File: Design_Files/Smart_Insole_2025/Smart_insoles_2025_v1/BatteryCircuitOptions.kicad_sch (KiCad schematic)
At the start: 23 parts, among them J4 S2B-PH-SM4-TB_LF__SN_, Q2 FDN306P, U1 ME6211C33M5, U7 BQ24040DSQR

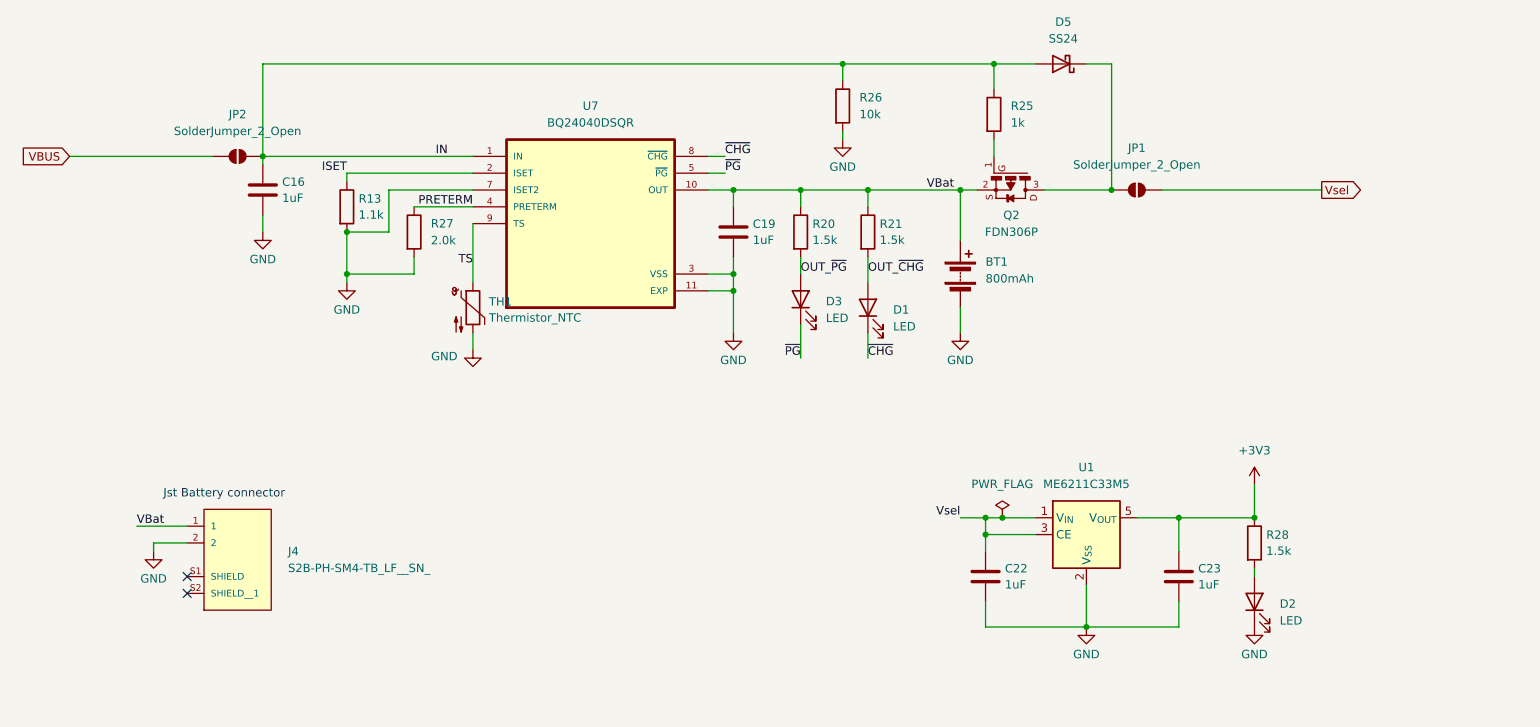
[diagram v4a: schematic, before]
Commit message: SCH: Added test points on idle MCU pins and Power supply. Added ON/OFF switch on VSEL.
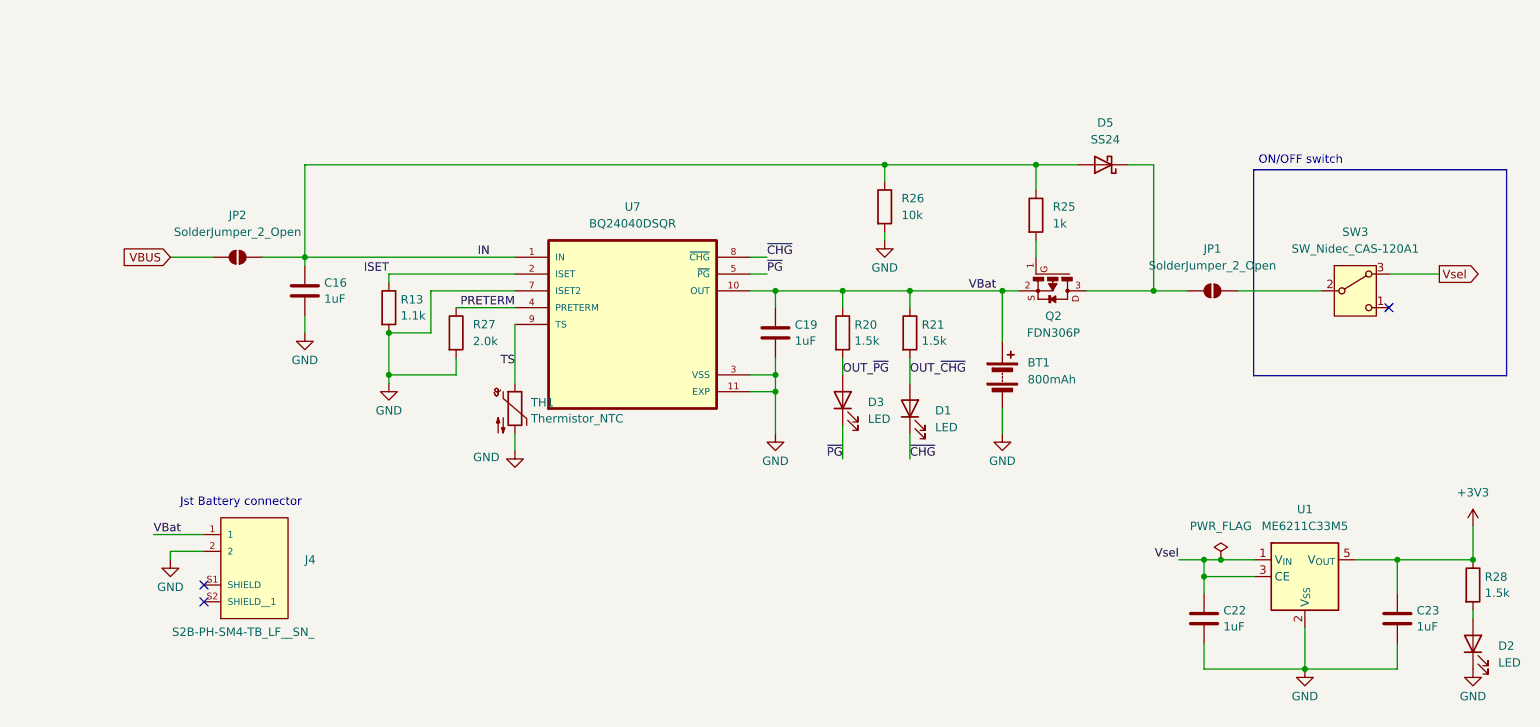
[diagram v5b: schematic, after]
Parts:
- added SW3: SW_Nidec_CAS-120A1, Button_Switch_SMD:Nidec_Copal_CAS-120A, symbol Switch:SW_Nidec_CAS-120A1
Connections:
- net Vsel: now also SW3.3 (A); no longer JP1.2 (B)
- new net: JP1.2 (B), SW3.2 (B)
- no-connect marks 2 -> 3
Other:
- note added: "ON/OFF switch"
- moved on the sheet: BT1, C16, C19, C22, C23, D1, D2, D3, D5, J4, JP1, JP2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

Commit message: PCB: Added 3d models to all components. Also preliminar routing of componentes. Component placemente needs checking.
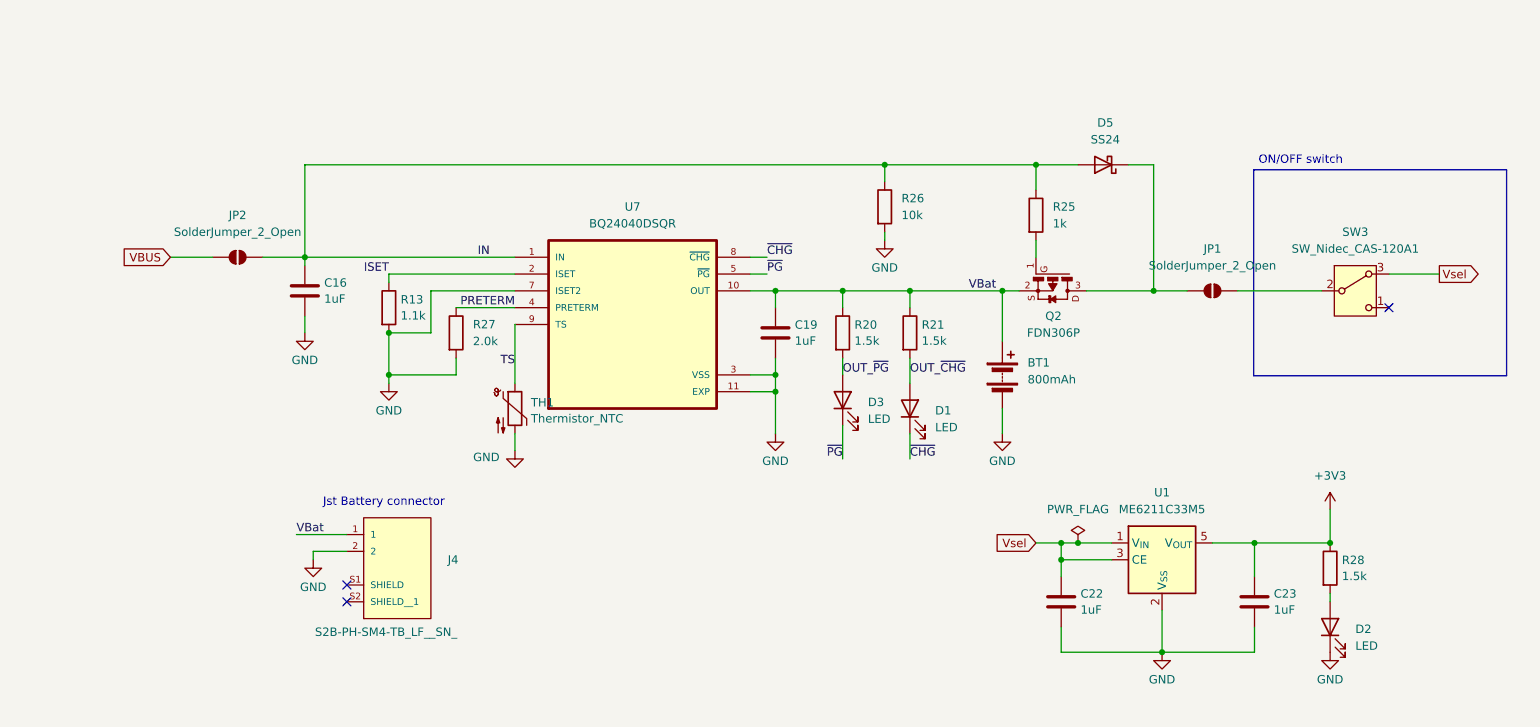
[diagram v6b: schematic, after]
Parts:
- SW3: footprint Button_Switch_SMD:Nidec_Copal_CAS-120A -> Button_Switch_SMD:SW_SPDT_PCM12
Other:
- moved on the sheet: C22, C23, D2, J4, R28, U1

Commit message: PCB:Routing missing connection. Still some missing
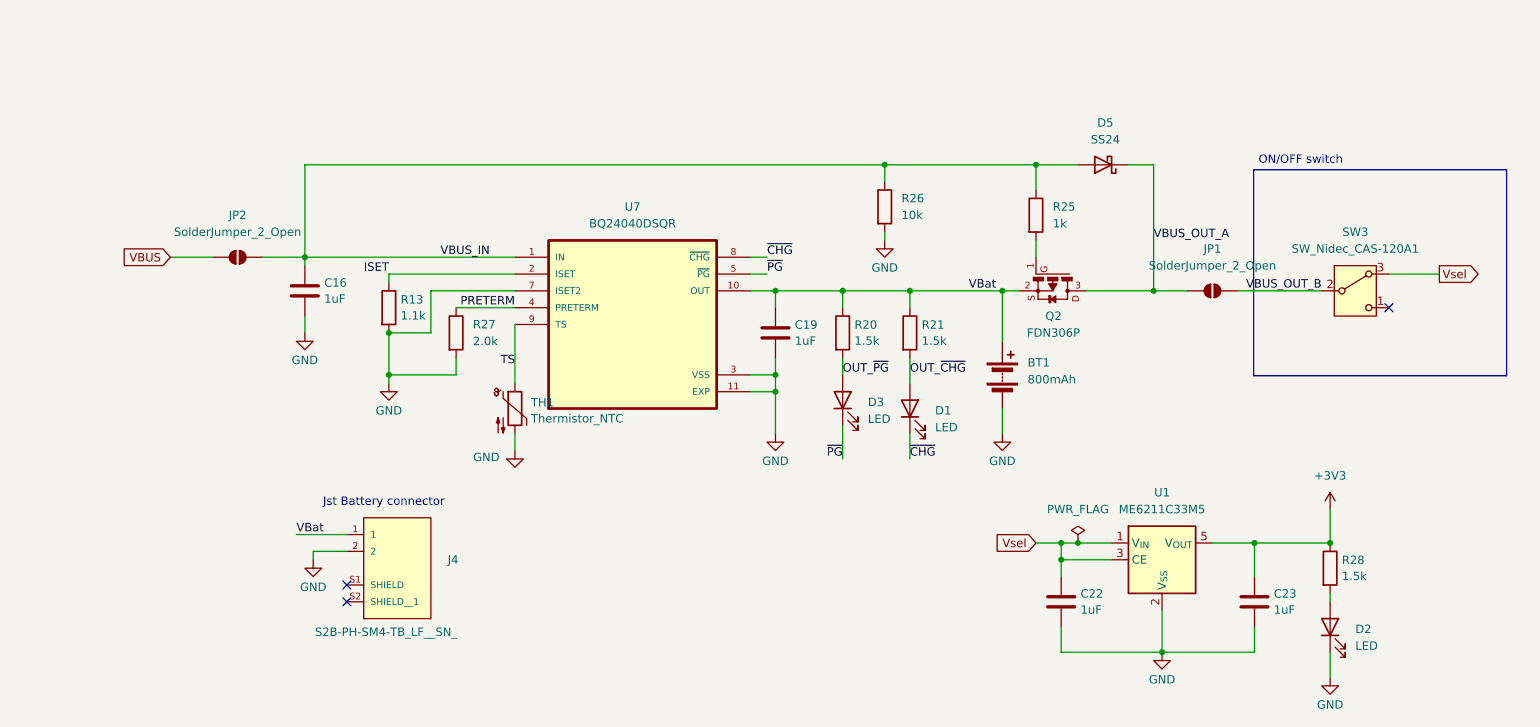
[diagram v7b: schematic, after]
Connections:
- net VBUS_OUT_A: now reaches D5.1 (K), JP1.1 (A), Q2.3
- net VBUS_OUT_B: now reaches JP1.2 (B), SW3.2 (B)
- net IN renamed VBUS_IN
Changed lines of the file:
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@@
+	(wire
+		(pts
+			(xy 227.33 129.54) (xy 227.33 125.73)
+		)
+		(stroke
+			(width 0)
+			(type default)
+		)
+	)
 	(wire
 		(pts
@@
 		)
 	)
-	(label "IN"
+	(label "VBUS_OUT_A"
+		(at 200.66 63.5 0)
+		(effects
+			(font
+				(size 1.27 1.27)
+			)
+			(justify left bottom)
+		)
+	)
+	(label "VBUS_IN"
 		(at 100.33 66.04 180)
 		(effects
@@
 			)
 			(justify right bottom)
+		)
+	)
+	(label "VBUS_OUT_B"
+		(at 214.63 71.12 0)
+		(effects
+			(font
+				(size 1.27 1.27)
+			)
+			(justify left bottom)
 		)
 	)
@@
 	(symbol
 		(lib_id "power:GND")
-		(at 227.33 125.73 0)
+		(at 227.33 129.54 0)
 		(unit 1)
 		(exclude_from_sim no)
@@
 		(fields_autoplaced yes)
 		(property "Reference" "#PWR055"
-			(at 227.33 132.08 0)
+			(at 227.33 135.89 0)
 			(effects
 				(font
@@
 		)
 		(property "Value" "GND"
-			(at 227.33 129.8631 0)
+			(at 227.33 133.6731 0)
 			(effects
 				(font
@@
 		)
 		(property "Footprint" ""
-			(at 227.33 125.73 0)
+			(at 227.33 129.54 0)
 			(effects
 				(font
@@
 		)
 		(property "Datasheet" ""
-			(at 227.33 125.73 0)
+			(at 227.33 129.54 0)
 			(effects
 				(font
@@
 		)
 		(property "Description" "Power symbol creates a global label with name \"GND\" , ground"
-			(at 227.33 125.73 0)
-			(effects
-				(font
+			(at 227.33 129.54 0)
+			(effects
+				(font

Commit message: SCH:Added pullup resistors on strapping pins.Added 0.1uF on analog input. Added testpoint on missing pad. PCB:Placed new components.Routing refactoring p1
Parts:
- SW3: footprint Button_Switch_SMD:SW_SPDT_PCM12 -> Button_Switch_THT:SW_Slide-03_Wuerth-WS-SLTV_10x2.5x6.4_P2.54mm
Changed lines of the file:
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@@
 			)
 		)
-		(property "Footprint" "Button_Switch_SMD:SW_SPDT_PCM12"
+		(property "Footprint" "Button_Switch_THT:SW_Slide-03_Wuerth-WS-SLTV_10x2.5x6.4_P2.54mm"
 			(at 231.14 81.28 0)
 			(effects
@@
 					(reference "SW3")
 					(unit 1)
+				)
+				(path "/f1f3d712-154d-4111-a7c4-f47541abccf8/b19f5448-2243-4e3e-9dc2-3dfe205a5c07"
+					(reference "SW3")
+					(unit 1)
